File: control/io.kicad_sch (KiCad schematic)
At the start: 0 parts

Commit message: Temp Sensor BME280 added to IO control
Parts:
- added U2: BME280, Package_LGA:Bosch_LGA-8_2.5x2.5mm_P0.65mm_ClockwisePinNumbering, symbol Sensor:BME280
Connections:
- new net +3V3: U2.6 (VDDIO), U2.8 (VDD)
- new net CSB: U2.2 (CSB)
- new net GND: U2.1 (GND), U2.7 (GND)
- new net SCK: U2.4 (SCK)
- new net SDI: U2.3 (SDI)
- new net SDO: U2.5 (SDO)
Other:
- note added: "Temp sensor Depth sensor? (Water level in tank) - or water sensor ^ Or ultrasonic sensor?? (bounces off surface of water in bucket) Alt: water pump (turn power ON/OFF) & water filter (dist. to daughters)"

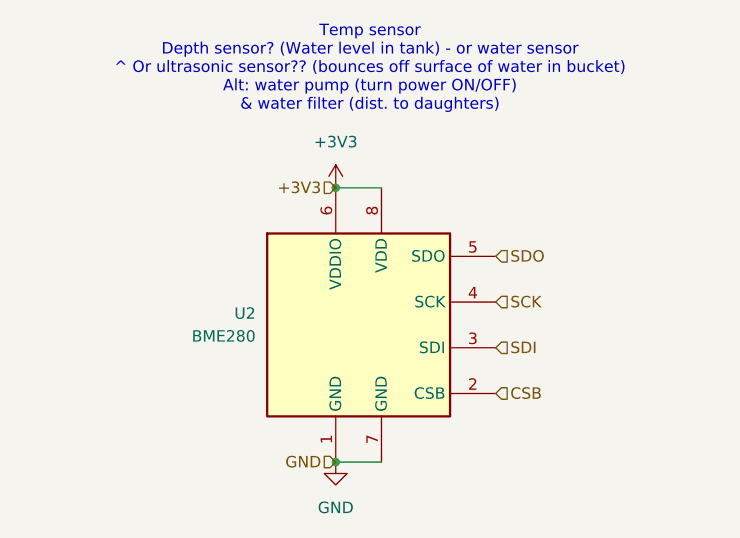
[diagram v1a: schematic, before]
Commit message: Component selection and BME280 cleanup
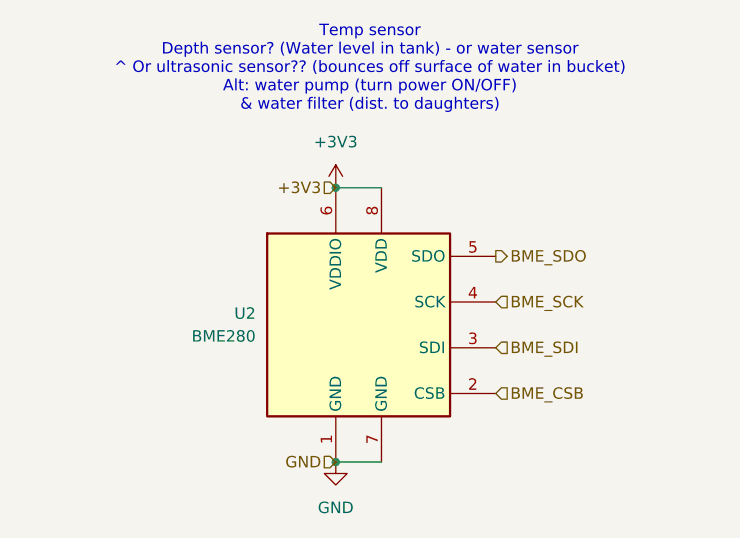
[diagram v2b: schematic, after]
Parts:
- U2: PN (none) -> BME280
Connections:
- net CSB renamed BME_CSB
- net SCK renamed BME_SCK
- net SDI renamed BME_SDI
- net SDO renamed BME_SDO
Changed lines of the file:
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@@
 		)
 	)
-	(hierarchical_label "SDI"
+	(hierarchical_label "BME_SDI"
 		(shape input)
 		(at 90.17 96.52 0)
@@
 		)
 	)
-	(hierarchical_label "SCK"
+	(hierarchical_label "BME_SCK"
 		(shape input)
 		(at 90.17 91.44 0)
@@
 		)
 	)
-	(hierarchical_label "SDO"
-		(shape input)
+	(hierarchical_label "BME_SDO"
+		(shape output)
 		(at 90.17 86.36 0)
 		(fields_autoplaced yes)
@@
 		)
 	)
-	(hierarchical_label "CSB"
+	(hierarchical_label "BME_CSB"
 		(shape input)
 		(at 90.17 101.6 0)
@@
 			(at 74.93 93.98 0)
 			(effects
+				(font
+					(size 1.27 1.27)
+				)
+				(hide yes)
+			)
+		)
+		(property "PN" "BME280"
+			(at 74.93 93.98 0)
+			(effects

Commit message: decoupling cap
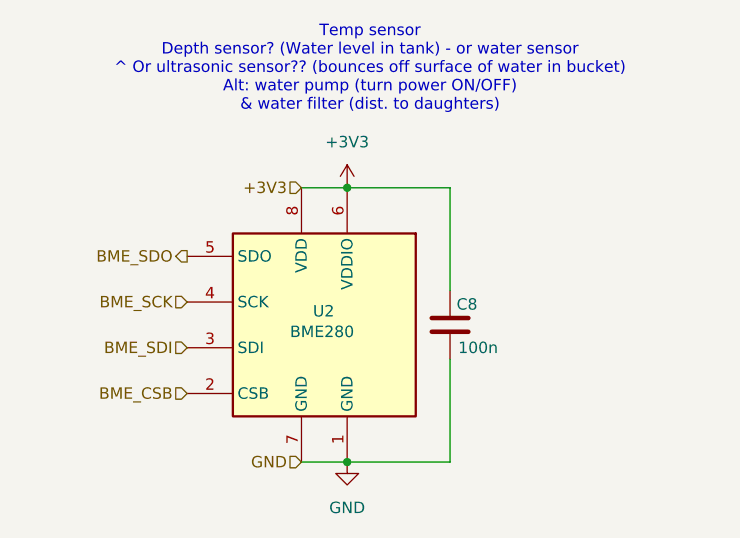
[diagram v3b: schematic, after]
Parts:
- added C8: 100n, Capacitor_SMD:C_0402_1005Metric_Pad0.74x0.62mm_HandSolder, symbol Device:C
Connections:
- net +3V3: now also C8.1
- net GND: now also C8.2
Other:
- moved on the sheet: U2
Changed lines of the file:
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@@
 	(paper "A4")
 	(junction
-		(at 72.39 109.22)
+		(at 73.66 109.22)
 		(diameter 0)
 		(color 0 0 0 0)
 	)
 	(junction
-		(at 72.39 78.74)
+		(at 73.66 78.74)
 		(diameter 0)
 		(color 0 0 0 0)
@@
 	(wire
 		(pts
-			(xy 72.39 78.74) (xy 77.47 78.74)
-		)
-		(stroke
-			(width 0)
-			(type default)
-		)
-	)
-	(wire
-		(pts
-			(xy 72.39 109.22) (xy 77.47 109.22)
+			(xy 85.09 97.79) (xy 85.09 109.22)
+		)
+		(stroke
+			(width 0)
+			(type default)
+		)
+	)
+	(wire
+		(pts
+			(xy 73.66 78.74) (xy 68.58 78.74)
+		)
+		(stroke
+			(width 0)
+			(type default)
+		)
+	)
+	(wire
+		(pts
+			(xy 73.66 109.22) (xy 68.58 109.22)
+		)
+		(stroke
+			(width 0)
+			(type default)
+		)
+	)
+	(wire
+		(pts
+			(xy 85.09 78.74) (xy 73.66 78.74)
+		)
+		(stroke
+			(width 0)
+			(type default)
+		)
+	)
+	(wire
+		(pts
+			(xy 85.09 109.22) (xy 73.66 109.22)
+		)
+		(stroke
+			(width 0)
+			(type default)
+		)
+	)
+	(wire
+		(pts
+			(xy 85.09 78.74) (xy 85.09 90.17)
 		)
 		(stroke
@@
 	(hierarchical_label "BME_SDI"
 		(shape input)
-		(at 90.17 96.52 0)
-		(fields_autoplaced yes)
-		(effects
-			(font
-				(size 1.27 1.27)
-			)
-			(justify left)
+		(at 55.88 96.52 180)
+		(fields_autoplaced yes)
+		(effects
+			(font
+				(size 1.27 1.27)
+			)
+			(justify right)
 		)
 	)
 	(hierarchical_label "+3V3"
 		(shape input)
-		(at 72.39 78.74 180)
+		(at 68.58 78.74 180)
 		(fields_autoplaced yes)
 		(effects
@@
 	(hierarchical_label "BME_SCK"
 		(shape input)
-		(at 90.17 91.44 0)
-		(fields_autoplaced yes)
-		(effects
-			(font
-				(size 1.27 1.27)
-			)
-			(justify left)
+		(at 55.88 91.44 180)
+		(fields_autoplaced yes)
+		(effects
+			(font
+				(size 1.27 1.27)
+			)
+			(justify right)
 		)
 	)
 	(hierarchical_label "BME_SDO"
 		(shape output)
-		(at 90.17 86.36 0)
-		(fields_autoplaced yes)
-		(effects
-			(font
-				(size 1.27 1.27)
-			)
-			(justify left)
+		(at 55.88 86.36 180)
+		(fields_autoplaced yes)
+		(effects
+			(font
+				(size 1.27 1.27)
+			)
+			(justify right)
 		)
 	)
 	(hierarchical_label "GND"
 		(shape input)
-		(at 72.39 109.22 180)
+		(at 68.58 109.22 180)
 		(fields_autoplaced yes)
 		(effects
@@
 	(hierarchical_label "BME_CSB"
 		(shape input)
-		(at 90.17 101.6 0)
-		(fields_autoplaced yes)
-		(effects
-			(font
-				(size 1.27 1.27)
-			)
-			(justify left)
+		(at 55.88 101.6 180)
+		(fields_autoplaced yes)
+		(effects
+			(font
+				(size 1.27 1.27)
+			)
+			(justify right)
 		)
 	)
 	(symbol
-		(lib_id "power:GND")
-		(at 72.39 109.22 0)
+		(lib_id "Device:C")
+		(at 85.09 93.98 0)
+		(mirror y)
 		(unit 1)
 		(exclude_from_sim no)
@@
 		(on_board yes)
 		(dnp no)
+		(property "Reference" "C8"
+			(at 88.138 91.694 0)
+			(effects
+				(font
+					(size 1.27 1.27)
+				)
+				(justify left)
+			)
+		)
+		(property "Value" "100n"
+			(at 90.424 96.52 0)
+			(effects
+				(font
+					(size 1.27 1.27)
+				)
+				(justify left)
+			)
+		)
+		(property "Footprint" "Capacitor_SMD:C_0402_1005Metric_Pad0.74x0.62mm_HandSolder"
+			(at 84.1248 97.79 0)
+			(effects
+				(font
+					(size 1.27 1.27)
+				)
+				(hide yes)
+			)
+		)
+		(property "Datasheet" "~"
+			(at 85.09 93.98 0)
+			(effects
+				(font
+					(size 1.27 1.27)
+				)
+				(hide yes)
+			)
+		)
+		(property "Description" "Unpolarized capacitor"
+			(at 85.09 93.98 0)
+			(effects
+				(font
+					(size 1.27 1.27)
+				)
+				(hide yes)
+			)
+		)
+		(property "PN" "GCM155R71C104KA55D"
+			(at 85.09 93.98 0)
+			(effects
+				(font
+					(size 1.27 1.27)
+				)
+				(hide yes)
+			)
+		)
+		(pin "2"
+		)
+		(pin "1"
+		)
+		(instances
+			(project ""
+				(path "/f45f1ed7-9099-407f-b6ad-6cac15e7865f/aeaadb5d-d6ee-48d0-a23f-7fd6d0a8d282"
+					(reference "C8")
+					(unit 1)
+				)
+			)
+		)
+	)
+	(symbol
+		(lib_id "power:GND")
+		(at 73.66 109.22 0)
+		(mirror y)
+		(unit 1)
+		(exclude_from_sim no)
+		(in_bom yes)
+		(on_board yes)
+		(dnp no)
 		(fields_autoplaced yes)
 		(property "Reference" "#PWR017"
-			(at 72.39 115.57 0)
+			(at 73.66 115.57 0)
 			(effects
 				(font
@@
 		)
 		(property "Value" "GND"
-			(at 72.39 114.3 0)
+			(at 73.66 114.3 0)
 			(effects
 				(font
@@
 		)
 		(property "Footprint" ""
-			(at 72.39 109.22 0)
+			(at 73.66 109.22 0)
 			(effects
 				(font
@@
 		)
 		(property "Datasheet" ""
-			(at 72.39 109.22 0)
+			(at 73.66 109.22 0)
 			(effects
 				(font
@@
 		)
 		(property "Description" "Power symbol creates a global label with name \"GND\" , ground"
-			(at 72.39 109.22 0)
+			(at 73.66 109.22 0)
 			(effects
 				(font
@@
 	(symbol
 		(lib_id "power:+3V3")
-		(at 72.39 78.74 0)
+		(at 73.66 78.74 0)
+		(mirror y)
 		(unit 1)
 		(exclude_from_sim no)
@@
 		(fields_autoplaced yes)
 		(property "Reference" "#PWR016"
-			(at 72.39 82.55 0)
+			(at 73.66 82.55 0)
 			(effects
 				(font
@@
 		)
 		(property "Value" "+3V3"
-			(at 72.39 73.66 0)
+			(at 73.66 73.66 0)
 			(effects
 				(font
@@
 		)
 		(property "Footprint" ""
-			(at 72.39 78.74 0)
+			(at 73.66 78.74 0)
 			(effects
 				(font
@@
 		)
 		(property "Datasheet" ""
-			(at 72.39 78.74 0)
+			(at 73.66 78.74 0)
 			(effects
 				(font
@@
 		)
 		(property "Description" "Power symbol creates a global label with name \"+3V3\""
-			(at 72.39 78.74 0)
+			(at 73.66 78.74 0)
 			(effects
 				(font
@@
 	(symbol
 		(lib_id "Sensor:BME280")
-		(at 74.93 93.98 0)
+		(at 71.12 93.98 0)
+		(mirror y)
 		(unit 1)
 		(exclude_from_sim no)
@@
 		(on_board yes)
 		(dnp no)
-		(fields_autoplaced yes)
 		(property "Reference" "U2"
-			(at 63.5 92.7099 0)
+			(at 69.85 92.456 0)
 			(effects
 				(font
@@
 		)
 		(property "Value" "BME280"
-			(at 63.5 95.2499 0)
+			(at 67.31 94.742 0)
 			(effects
 				(font
@@
 		)
 		(property "Footprint" "Package_LGA:Bosch_LGA-8_2.5x2.5mm_P0.65mm_ClockwisePinNumbering"
-			(at 113.03 105.41 0)
+			(at 33.02 105.41 0)
 			(effects
 				(font
@@
 		)
 		(property "Datasheet" "https://www.bosch-sensortec.com/media/boschsensortec/downloads/datasheets/bst-bme280-ds002.pdf"
-			(at 74.93 99.06 0)
+			(at 71.12 99.06 0)
 			(effects
 				(font
@@
 		)
 		(property "Description" "3-in-1 sensor, humidity, pressure, temperature, I2C and SPI interface, 1.71-3.6V, LGA-8"
-			(at 74.93 93.98 0)
+			(at 71.12 93.98 0)
 			(effects
 				(font
@@
 		)
 		(property "PN" "BME280"
-			(at 74.93 93.98 0)
-			(effects
-				(font
+			(at 71.12 93.98 0)
+			(effects
+				(font
